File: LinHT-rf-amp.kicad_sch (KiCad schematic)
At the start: 24 parts, among them J1 INPUT, J2 OUTPUT, J4 SIGNALS, U1 GRF5604

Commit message: Added LCSC and manufacturer numbers for all components
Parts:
- C1, C3: LCSC (none) -> C464434; MP (none) -> GJM1555C1H330FB01D
- C10: LCSC (none) -> C913614; MP (none) -> GRM155C71H104KE19D
- C11, C12, C8: LCSC (none) -> C161523; MP (none) -> GRM1555C1H102FA01D
- C2: LCSC (none) -> C782046; MP (none) -> GJM1555C1H100FB01D
- C4: LCSC (none) -> C88896; MP (none) -> GJM1555C1H6R8BB01D
- C5: LCSC (none) -> C88883; MP (none) -> GJM1555C1H270FB01D
- C6: LCSC (none) -> C88891; MP (none) -> GJM1555C1H3R0BB01D
- C7: LCSC (none) -> C77177; MP (none) -> GRM1555C1H101JA01D
- C9: LCSC (none) -> C237279; MP (none) -> GRM155C80J106ME11D
- J1, J2, J4: now left out of the parts list
- L1: LCSC (none) -> C668375; MP (none) -> LQG15HH10NJ02D
- L2: LCSC (none) -> C2042508; MP (none) -> LQW18AN2N4C8ZD
- L3: footprint (none) -> Parts:0908SQ-23N; LCSC (none) -> C42418190 or C5441443; MP (none) -> XR0908SQ-23NJLC or 0908SQ-23NJLC
- L4: LCSC (none) -> C20623501; MP (none) -> 0402HP-20NXGLW
- R1: LCSC (none) -> C70427; MP (none) -> 0402WGF1961TCE
- R2: LCSC (none) -> C25913; MP (none) -> 0402WGF6041TCE
- R3: LCSC (none) -> C25741; MP (none) -> 0402WGF1003TCE
- U1: MP (none) -> GRF5604

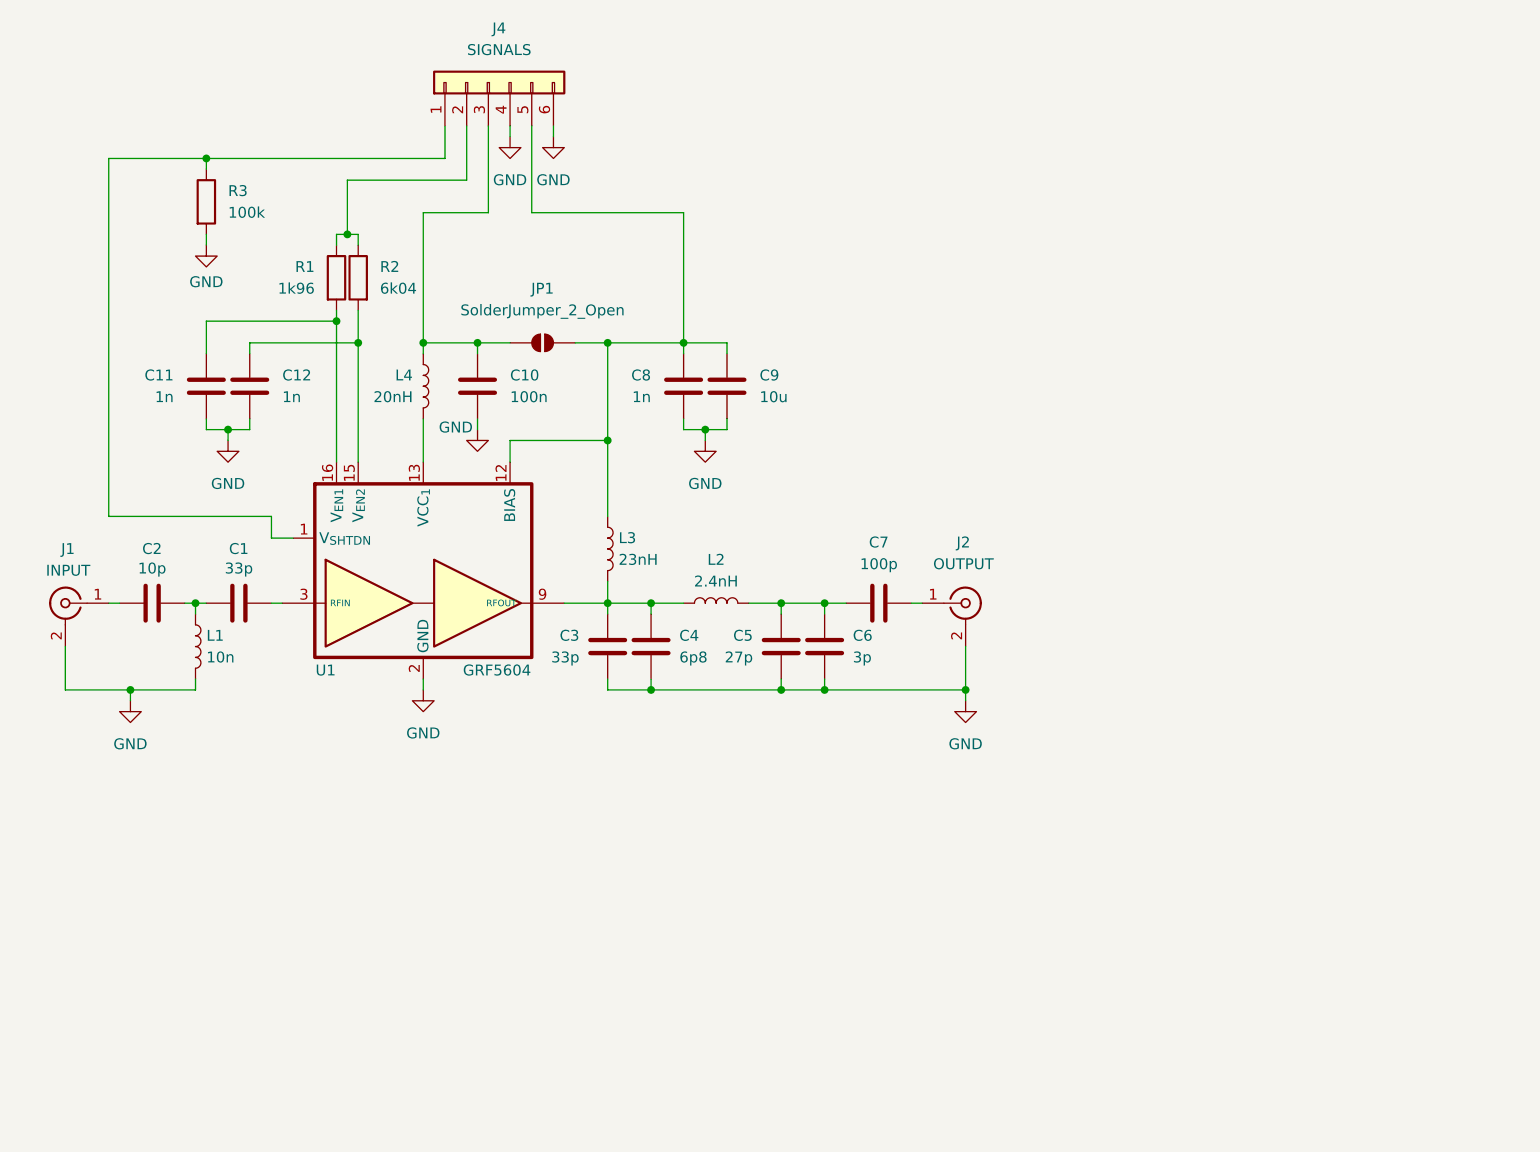
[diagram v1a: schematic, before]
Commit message: Added signal names to the schematics
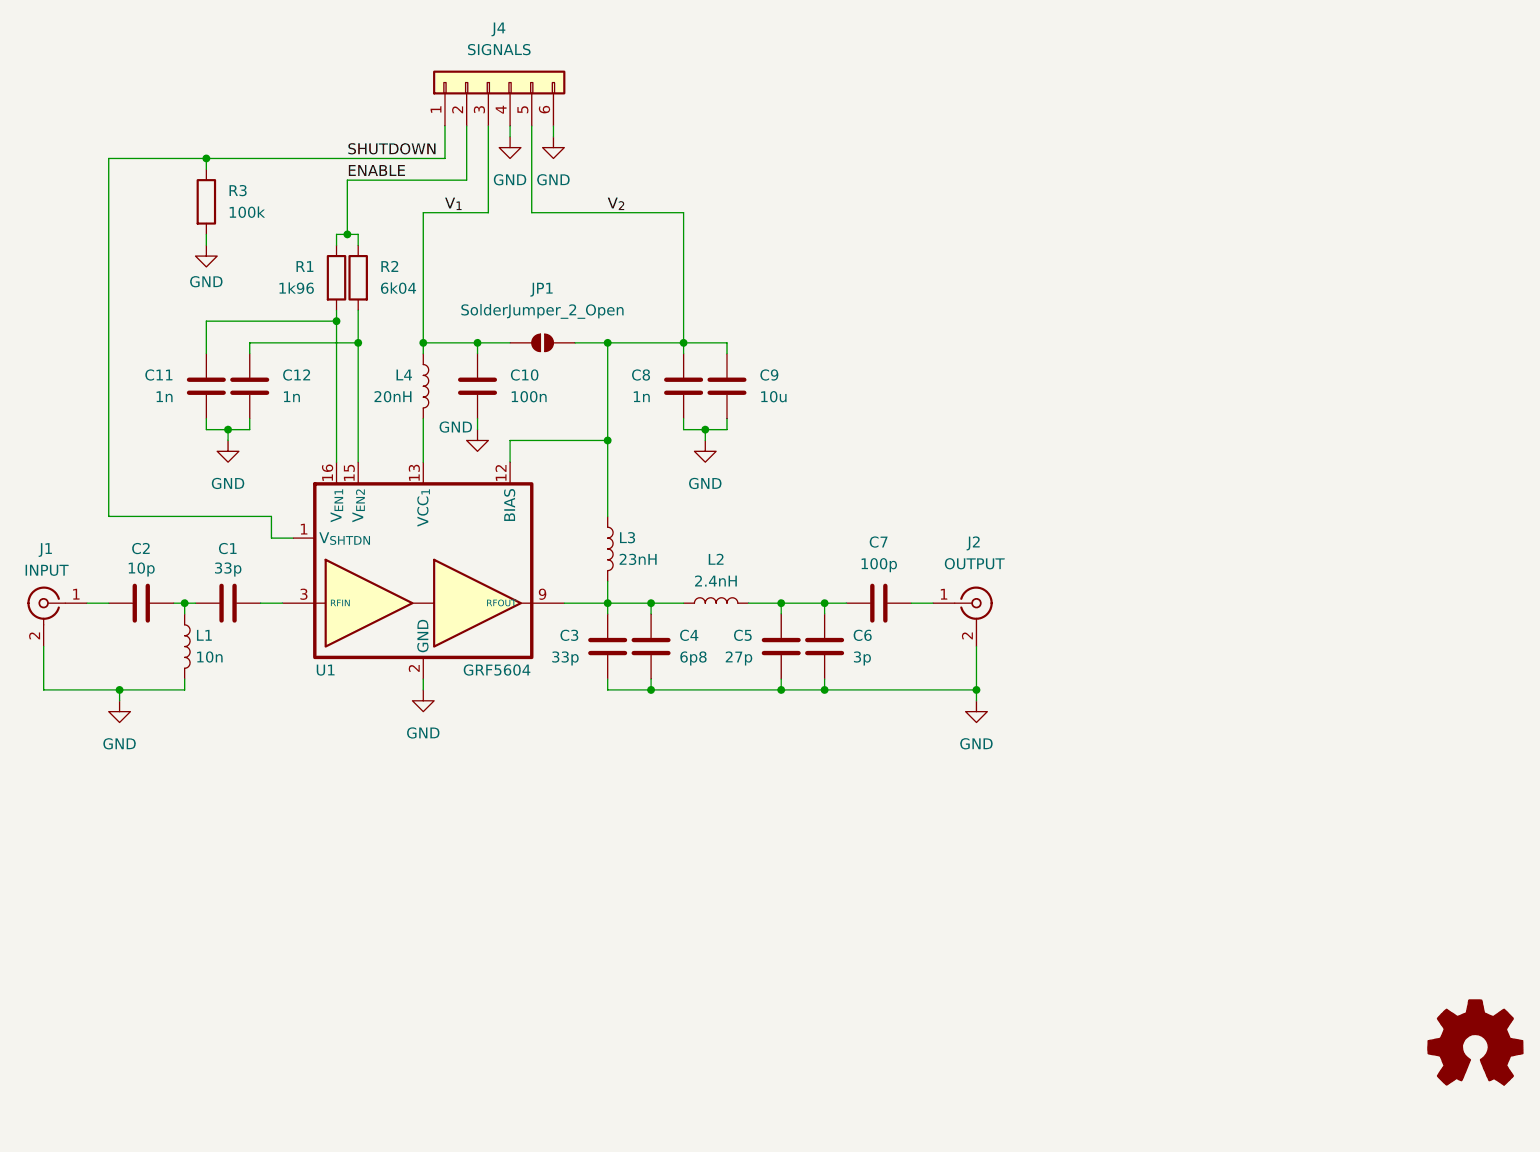
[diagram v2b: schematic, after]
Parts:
- added SYM1: Logo_Open_Hardware_Small, Symbol:OSHW-Logo2_7.3x6mm_SilkScreen, symbol Graphic:Logo_Open_Hardware_Small
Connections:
- net ENABLE: now reaches J4.2 (Pin_2), R1.1, R2.1
- net V_{2}: now reaches C8.2, C9.2, J4.5 (Pin_5), JP1.2 (B), L3.1, U1.12 (BIAS)
- net V_{1}: now reaches C10.2, J4.3 (Pin_3), JP1.1 (A), L4.1
- net SHUTDOWN: now reaches J4.1 (Pin_1), R3.1, U1.1 (V_{SHTDN})
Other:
- moved on the sheet: C1, C2, J1, J2, L1

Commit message: Fixed RF traces, reset annotation, added M2 holes
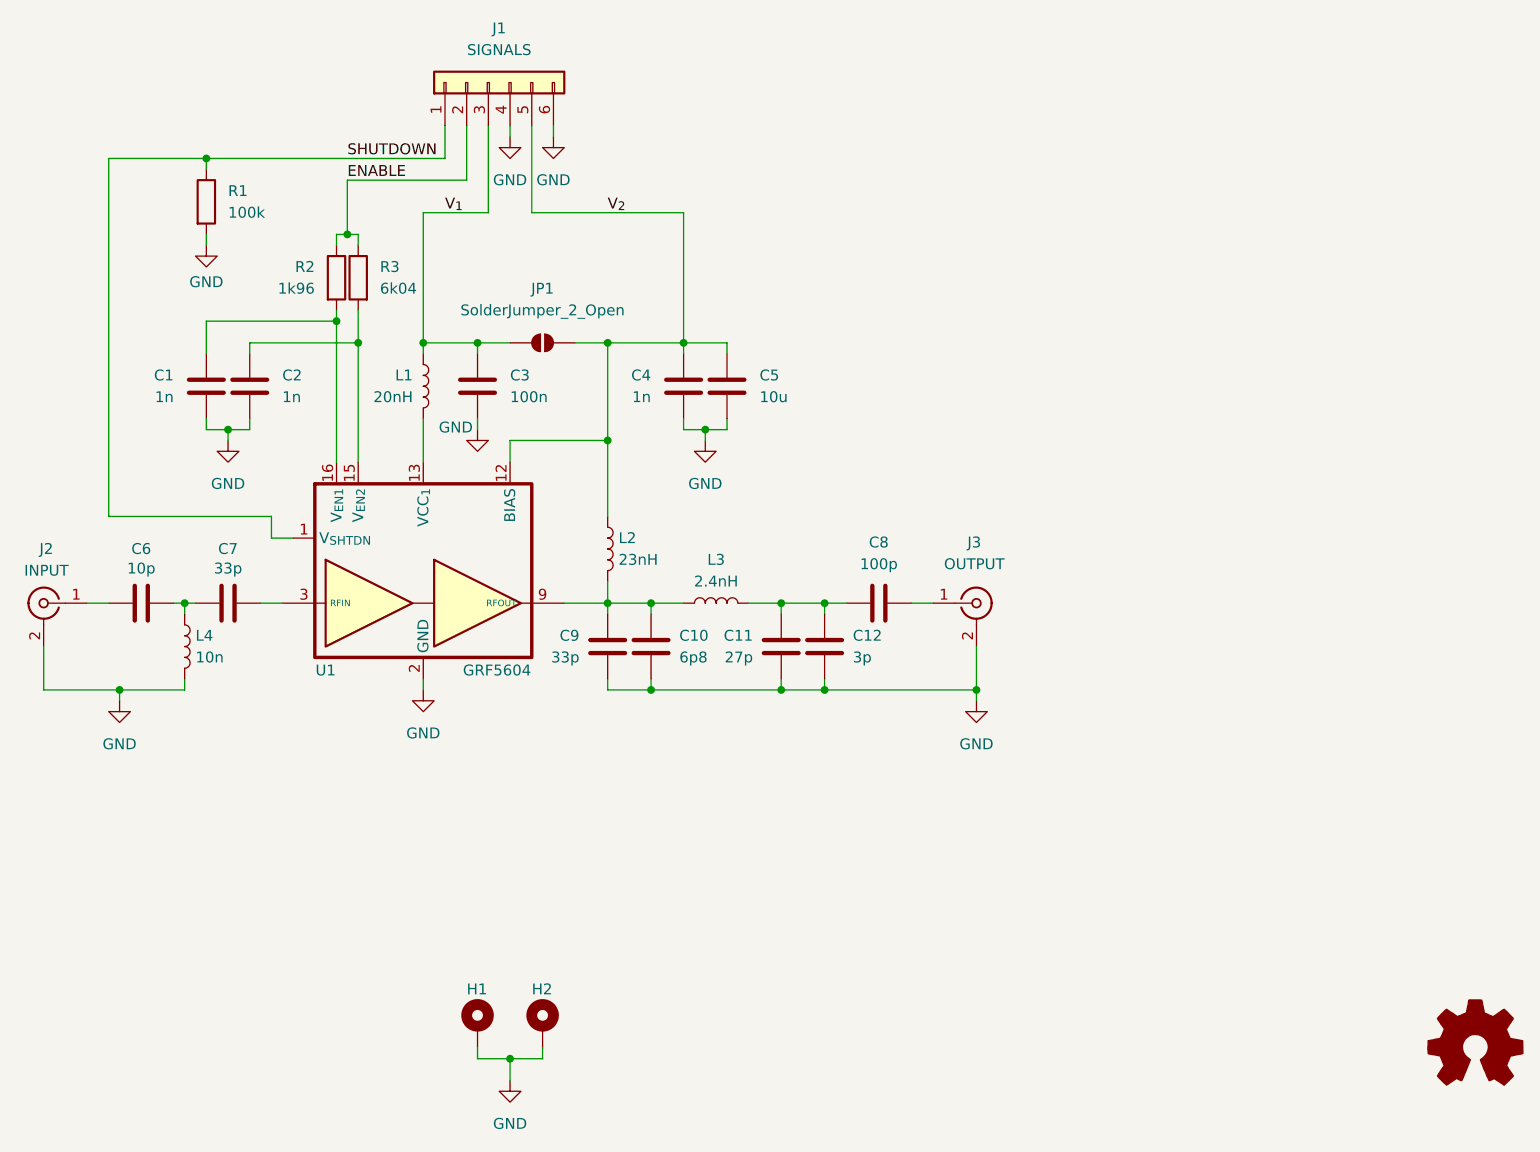
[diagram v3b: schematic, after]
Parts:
- added H1, H2: MountingHole_Pad_MP, MountingHole:MountingHole_2.2mm_M2_DIN965_Pad, symbol Mechanical:MountingHole_Pad
- renumbered C11 to C1, C4 to C10, C5 to C11, C6 to C12, C12 to C2, C10 to C3, C8 to C4, C9 to C5, C2 to C6, C1 to C7, C7 to C8, C3 to C9, J4 to J1, J1 to J2, J2 to J3, L4 to L1, L3 to L2, L2 to L3, L1 to L4, R3 to R1, R1 to R2, R2 to R3
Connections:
- net GND: now also H1.1, H2.1

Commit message: Added a low pass filter LFCN-490+
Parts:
- added FL1: LFCN-490, Filter:Filter_Mini-Circuits_FV1206, symbol RF_Filter:LFCN-490
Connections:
- net GND: now also FL1.2 (GND), FL1.4 (GND)
- net at J3.1 (In): now also FL1.3 (OUT); no longer C8.2
- new net: C8.2, FL1.1 (IN)
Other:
- moved on the sheet: J3

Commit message: Updated  design to use new GRF5604 footprint
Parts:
- U1: footprint Package_DFN_QFN:QFN-16-1EP_3x3mm_P0.5mm_EP1.7x1.7mm_ThermalVias -> Parts:QFN-16-1EP_3x3mm_P0.5mm_EP1.7x1.7mm_ThermalVias
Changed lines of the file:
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@@
 			)
 		)
-		(property "Footprint" "Package_DFN_QFN:QFN-16-1EP_3x3mm_P0.5mm_EP1.7x1.7mm_ThermalVias"
+		(property "Footprint" "Parts:QFN-16-1EP_3x3mm_P0.5mm_EP1.7x1.7mm_ThermalVias"
 			(at 150.622 135.382 0)
 			(effects

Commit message: Remove alternative part number for the L2 coil
Original Coilcraft coil 0908SQ-23NJLC is not easily available at LCSC,
so we chose the alternative part XR0908SQ-23NJLC with the same params.
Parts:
- L2: LCSC C42418190 or C5441443 -> C42418190; MP XR0908SQ-23NJLC or 0908SQ-23NJLC -> XR0908SQ-23NJLC
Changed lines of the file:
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@@
 			)
 		)
-		(property "LCSC" "C42418190 or C5441443"
+		(property "LCSC" "C42418190"
 			(at 161.29 115.57 0)
 			(effects
@@
 			)
 		)
-		(property "MP" "XR0908SQ-23NJLC or 0908SQ-23NJLC"
+		(property "MP" "XR0908SQ-23NJLC"
 			(at 161.29 115.57 0)
 			(effects

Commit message: title update
frequency range starts at 397 MHz
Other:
- title: LinHT - 390-470 MHz Power Amplifier -> LinHT - 397-470 MHz Power Amplifier
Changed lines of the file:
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@@
 	(paper "A4")
 	(title_block
-		(title "LinHT - 390-470 MHz Power Amplifier")
+		(title "LinHT - 397-470 MHz Power Amplifier")
 		(date "2025-08-18")
 		(rev "A")
